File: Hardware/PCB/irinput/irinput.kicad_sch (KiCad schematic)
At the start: 38 parts, among them J1 AudioJack3, J2 Synth_power_2x5, J3 Conn_01x06, J4 Conn_01x06, J5 AudioJack2, J6 AudioJack2, Q1 TOPS-050, SW1 SW_DPDT_x2, SW2 SW_SPDT, U1 TL074

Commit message: Revised schematic to buffer input to variable gain stage
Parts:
- removed C1: 1uF, ao_tht:C_Rect_L7.2mm_W7.2mm_P5.00mm_FKS2_FKP2_MKS2_MKP2, symbol ao_symbols:C
- removed J1: AudioJack3, ao_tht:Jack_6.35mm_PJ_629HAN, symbol ao_symbols:AudioJack3
- removed Q1: TOPS-050, ao_tht:LED_D5.0mm, symbol Device:Q_Photo_NPN
- removed R1: 100R, ao_tht:R_Axial_DIN0207_L6.3mm_D2.5mm_P10.16mm_Horizontal, symbol ao_symbols:R
- removed R12: 2.2k, ao_tht:R_Axial_DIN0207_L6.3mm_D2.5mm_P10.16mm_Horizontal, symbol ao_symbols:R
- removed R2: 10R, ao_tht:R_Axial_DIN0207_L6.3mm_D2.5mm_P10.16mm_Horizontal, symbol ao_symbols:R
- removed R3: 100k, ao_tht:R_Axial_DIN0207_L6.3mm_D2.5mm_P10.16mm_Horizontal, symbol ao_symbols:R
- removed R4: 10k, ao_tht:R_Axial_DIN0207_L6.3mm_D2.5mm_P10.16mm_Horizontal, symbol ao_symbols:R
- removed RV1: A1M, ao_tht:Potentiometer_Alpha_RD901F-40-00D_Single_Vertical_centered, symbol ao_symbols:R_POT
- removed SW2: SW_SPDT, ao_tht:SPDT-toggle-switch-1M-series, symbol ao_symbols:SW_SPDT
- removed unit 4 of U1
- added C?: 1uF, ao_tht:C_Rect_L7.2mm_W7.2mm_P5.00mm_FKS2_FKP2_MKS2_MKP2, symbol ao_symbols:C
- added H1, H2, H3, H4: MountingHole, ao_tht:MountingHole_3.2mm_M3, symbol ao_symbols:MountingHole
- added J?: AudioJack3, ao_tht:Jack_6.35mm_PJ_629HAN, symbol ao_symbols:AudioJack3
- added Q?: TOPS-050, ao_tht:LED_D5.0mm, symbol Device:Q_Photo_NPN
- added R?: 100R, ao_tht:R_Axial_DIN0207_L6.3mm_D2.5mm_P10.16mm_Horizontal, symbol ao_symbols:R
- added R?: 10k, ao_tht:R_Axial_DIN0207_L6.3mm_D2.5mm_P10.16mm_Horizontal, symbol ao_symbols:R
- added R? (x2): 100k, ao_tht:R_Axial_DIN0207_L6.3mm_D2.5mm_P10.16mm_Horizontal, symbol ao_symbols:R
- added R?: 10R, ao_tht:R_Axial_DIN0207_L6.3mm_D2.5mm_P10.16mm_Horizontal, symbol ao_symbols:R
- added RV?: A1M, ao_tht:Potentiometer_Alpha_RD901F-40-00D_Single_Vertical_centered, symbol ao_symbols:R_POT
- added SW2: SW_DPDT_x2, ao_tht:DPDT-toggle-switch-1M-seriesx, symbol Switch:SW_DPDT_x2
- added U?: TL074, ao_tht:DIP-14_W7.62mm_Socket_LongPads, symbol ao_symbols:TL074
- R5, R6: value 10k -> 1k
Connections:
- net EMIT is gone; now on net DC: SW1.5 (B)
- net +12V: now also R?.1
- net AC: now also R?.1, SW2.3 (C)
- net COLL: now also R?.2
- net CV_LED_1: now also U1.14
- net CV_LED_1_P: now also D5.1 (KA); no longer D5.2 (AK)
- net CV_LED_2: now also R6.1, R8.1, U1.9 (-)
- net CV_LED_2_P: now also D5.2 (AK); no longer D5.1 (KA)
- net DC: now also C?.1, R?.1, SW2.1 (A)
- net EXT_C: now also J?.T
- net EXT_E: now also J?.R
- net GND: now also U1.12 (+), J?.S, R?.2, RV?.1; no longer U1.3 (+)
- net SENSITIVITY: now also R?.2, RV?.2, RV?.3
- net at RV2.2, RV2.3, U1.6 (-): now also R?.1, R?.1
- net at SW1.1 (A): now also Q?.1 (C)
- net at R5.1, R6.2: now also U1.13 (-); no longer U1.2 (-)
- net at SW1.4 (A): now also Q?.2 (E)
- new net: C?.2, SW2.2 (B), U?.3 (+)
- new net: R?.2, SW2.6 (C)
- new net: R?.2, SW2.4 (A)
- new net BUF: SW2.5 (B), U?.1, U?.2 (-)
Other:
- note added: "Inverting stages with variable gain added"
- note added: "Jacks/LEDs board"
- note removed: "Originally was fixed unity gain"
- moved on the sheet: D3, D4, D5, J3, J4, J5, J6, R10, R11, R5, R6, R7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

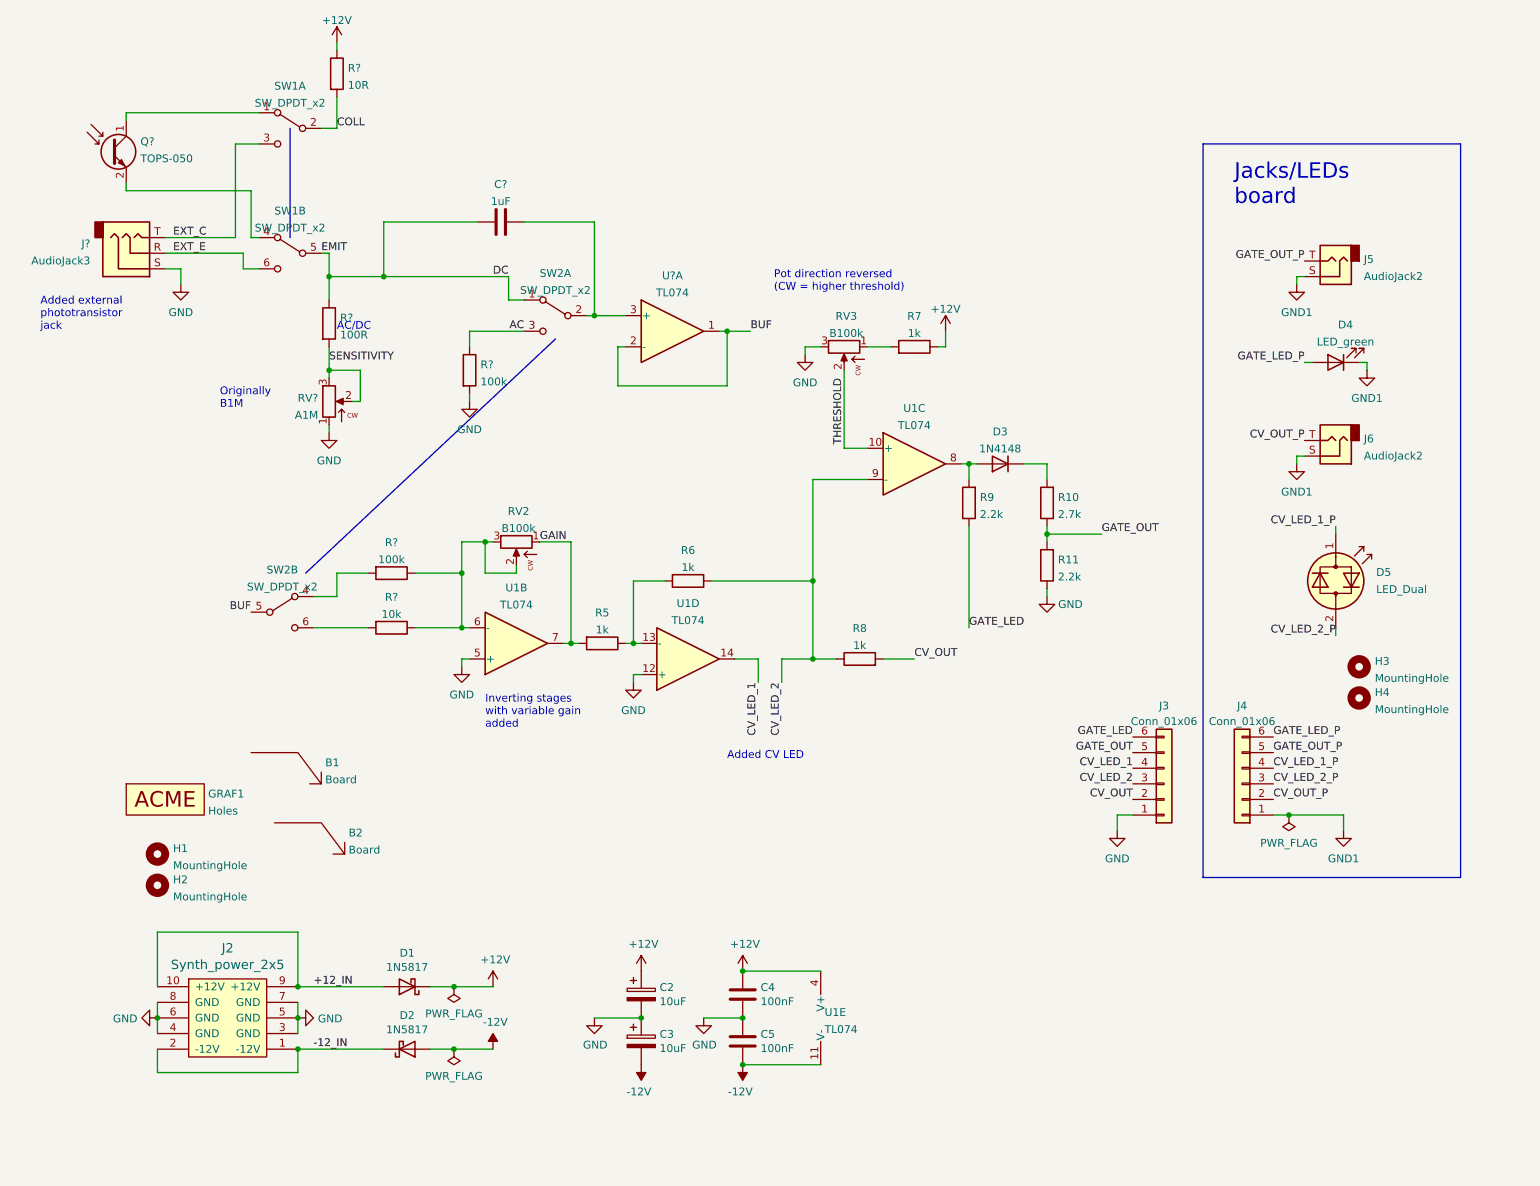
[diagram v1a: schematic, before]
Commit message: Revert to using no inverting stages, put gain control on non inverting stage. Add saturation LED.
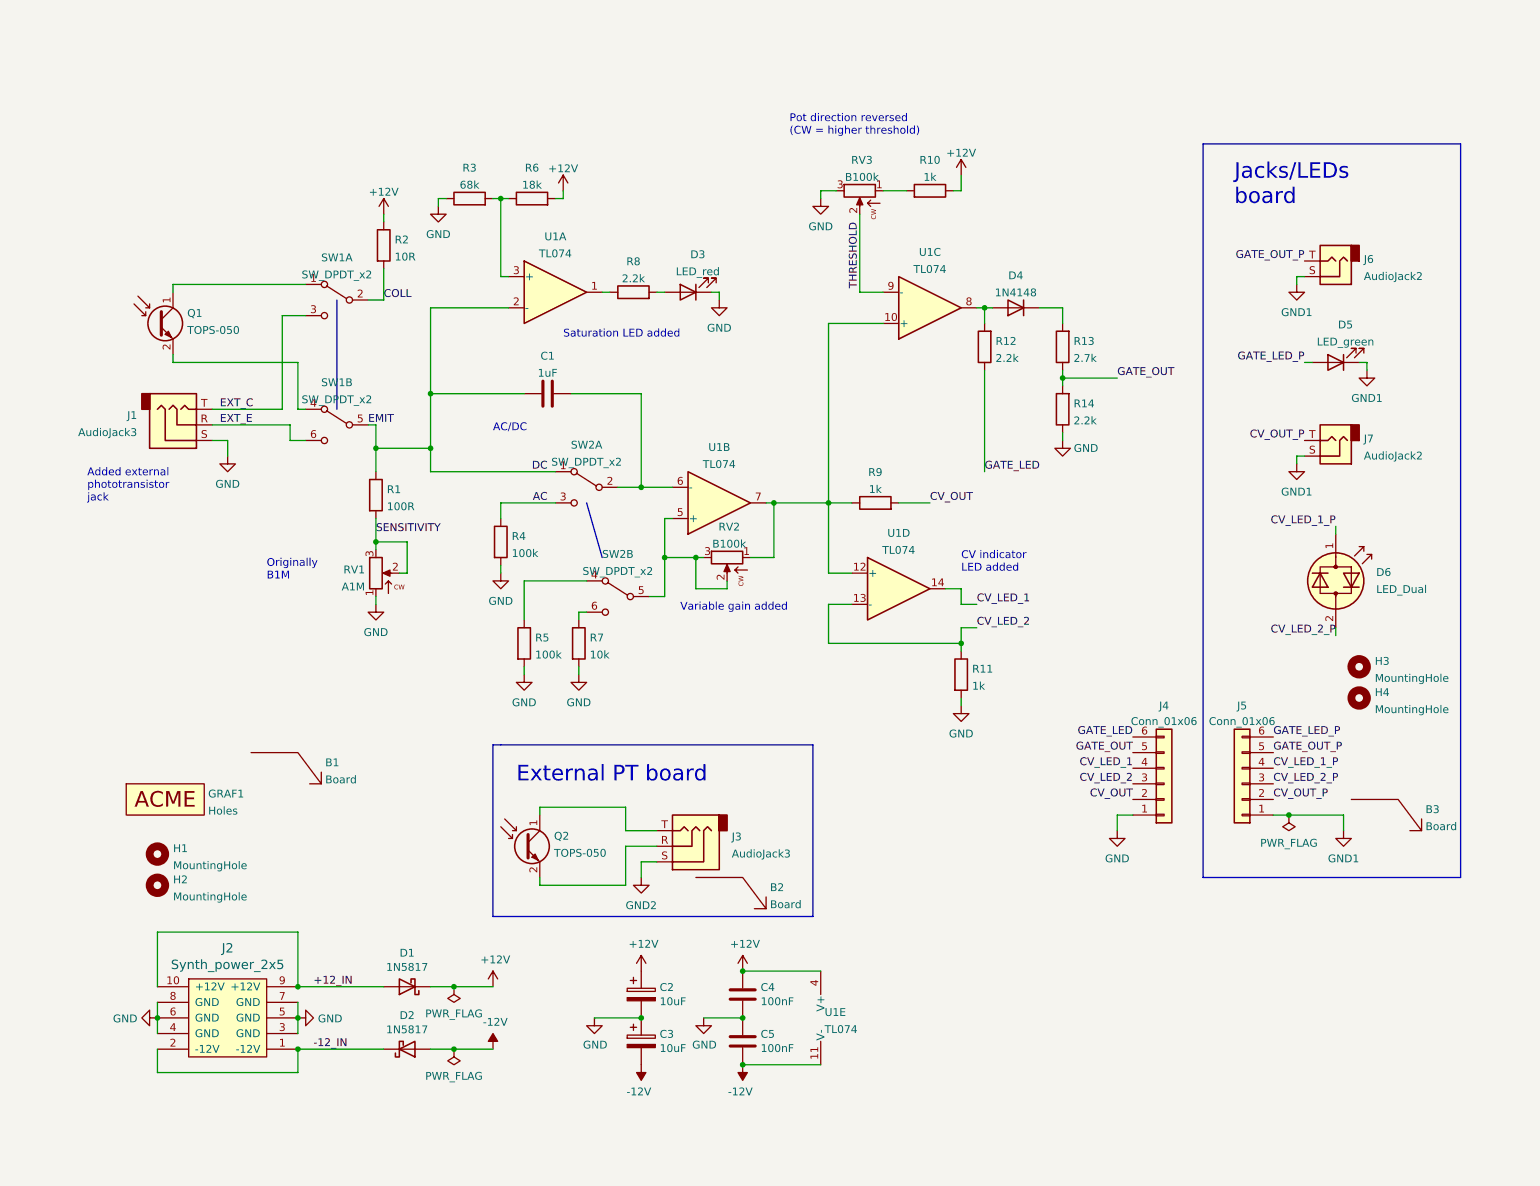
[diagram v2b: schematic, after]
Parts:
- removed R?: 10k, ao_tht:R_Axial_DIN0207_L6.3mm_D2.5mm_P10.16mm_Horizontal, symbol ao_symbols:R
- removed R?: 100k, ao_tht:R_Axial_DIN0207_L6.3mm_D2.5mm_P10.16mm_Horizontal, symbol ao_symbols:R
- added B2: Board, ao_tht:Board_Marker, symbol ao_symbols:Board
- added D3: LED_red, ao_tht:LED_D5.0mm, symbol ao_symbols:LED_red
- added J3: AudioJack3, ao_tht:Jack_3.5mm_PJ-301CM, symbol ao_symbols:AudioJack3
- added Q2: TOPS-050, ao_tht:LED_D5.0mm, symbol Device:Q_Photo_NPN
- added R11: 1k, ao_tht:R_Axial_DIN0207_L6.3mm_D2.5mm_P10.16mm_Horizontal, symbol ao_symbols:R
- added R3: 68k, ao_tht:R_Axial_DIN0207_L6.3mm_D2.5mm_P10.16mm_Horizontal, symbol ao_symbols:R
- added R7: 10k, ao_tht:R_Axial_DIN0207_L6.3mm_D2.5mm_P10.16mm_Horizontal, symbol ao_symbols:R
- added R8: 2.2k, ao_tht:R_Axial_DIN0207_L6.3mm_D2.5mm_P10.16mm_Horizontal, symbol ao_symbols:R
- J1: renamed from J?; footprint ao_tht:Jack_6.35mm_PJ_629HAN -> ao_tht:Jack_3.5mm_PJ-301CM
- R5: value 1k -> 100k
- R6: value 1k -> 18k
- gave numbers to parts that had none: 7
- renumbered B2 to B3, D3 to D4, D4 to D5, D5 to D6, J3 to J4, J4 to J5, J5 to J6, J6 to J7, R7 to R10, R9 to R12, R10 to R13, R11 to R14, R8 to R9
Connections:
- net +12V: now also R6.2
- net CV_LED_2: now also U1.13 (-), R11.1; no longer R6.1, R9.1, U1.9 (-)
- net DC: now also U1.2 (-)
- net GND: now also R5.2, D3.1 (K), R11.2, R3.1, R7.2; no longer U1.12 (+), U1.5 (+)
- net THRESHOLD: now also U1.9 (-); no longer U1.10 (+)
- net at C1.2, SW2.2 (B): now also U1.6 (-); no longer U1.3 (+)
- net at RV2.2, RV2.3: now also SW2.5 (B), U1.5 (+); no longer U1.6 (-)
- net at SW2.6 (C): now also R7.1
- net at SW2.4 (A): now also R5.1
- removed net BUF: SW2.5 (B), U1.1, U1.2 (-)
- net GAIN: no longer names the net of RV2.1, U1.7
- net GAIN: now also R9.1, U1.10 (+), U1.12 (+); no longer R5.2
- new net: R8.1, U1.1
- new net: R3.2, R6.1, U1.3 (+)
- new net: D3.2 (A), R8.2
- new net: J3.R, Q2.2 (E)
- new net: J3.T, Q2.1 (C)
- new net GND2: J3.S
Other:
- note added: "CV indicator LED added"
- note added: "External PT board"
- note added: "Saturation LED added"
- note added: "Variable gain added"
- note removed: "Added CV LED"
- note removed: "Inverting stages with variable gain added"
- moved on the sheet: B3, C1, D4, J1, Q1, R1, R10, R12, R13, R14, R2, R4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

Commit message: Corrections
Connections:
- net DC: now also U1.3 (+); no longer U1.2 (-)
- net at R3.2, R6.1: now also U1.2 (-); no longer U1.3 (+)
- net at C1.2, SW2.2 (B): now also U1.5 (+); no longer U1.6 (-)
- net at RV2.2, RV2.3, SW2.5 (B): now also U1.6 (-); no longer U1.5 (+)
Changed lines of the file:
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@@
     )
   )
-  (symbol (lib_id "ao_symbols:TL074") (at 104.14 59.69 0) (unit 1)
+  (symbol (lib_id "ao_symbols:TL074") (at 104.14 59.69 0) (mirror x) (unit 1)
     (in_bom yes) (on_board yes) (fields_autoplaced)
     (property "Reference" "U1" (id 0) (at 104.14 50.6435 0))
     (property "Value" "TL074" (id 1) (at 104.14 53.4186 0))
-    (property "Footprint" "ao_tht:DIP-14_W7.62mm_Socket_LongPads" (id 2) (at 102.87 57.15 0)
-      (effects (font (size 1.27 1.27)) hide)
-    )
-    (property "Datasheet" "" (id 3) (at 105.41 54.61 0)
+    (property "Footprint" "ao_tht:DIP-14_W7.62mm_Socket_LongPads" (id 2) (at 102.87 62.23 0)
+      (effects (font (size 1.27 1.27)) hide)
+    )
+    (property "Datasheet" "" (id 3) (at 105.41 64.77 0)
       (effects (font (size 1.27 1.27)) hide)
     )
@@
     (pin "1")
   )
-  (symbol (lib_id "ao_symbols:TL074") (at 130.81 93.98 0) (mirror x) (unit 2)
+  (symbol (lib_id "ao_symbols:TL074") (at 130.81 93.98 0) (unit 2)
     (in_bom yes) (on_board yes) (fields_autoplaced)
     (property "Reference" "U1" (id 0) (at 130.81 84.9335 0))
     (property "Value" "TL074" (id 1) (at 130.81 87.7086 0))
-    (property "Footprint" "ao_tht:DIP-14_W7.62mm_Socket_LongPads" (id 2) (at 129.54 96.52 0)
-      (effects (font (size 1.27 1.27)) hide)
-    )
-    (property "Datasheet" "" (id 3) (at 132.08 99.06 0)
-      (effects (font (size 1.27 1.27)) hide)
-    )
+    (property "Footprint" "ao_tht:DIP-14_W7.62mm_Socket_LongPads" (id 2) (at 129.54 91.44 0)
+      (effects (font (size 1.27 1.27)) hide)
+    )
+    (property "Datasheet" "" (id 3) (at 132.08 88.9 0)
+      (effects (font (size 1.27 1.27)) hide)
+    )

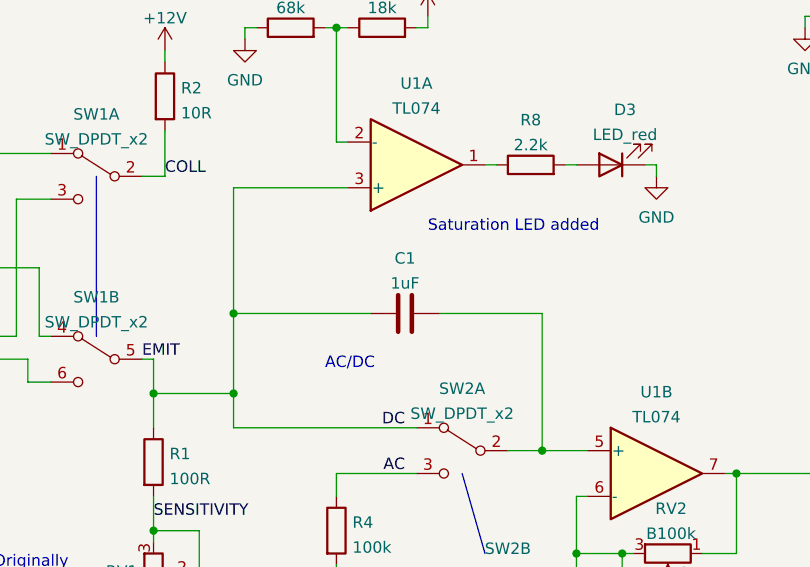
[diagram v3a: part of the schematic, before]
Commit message: Corrected cap, initial BOM
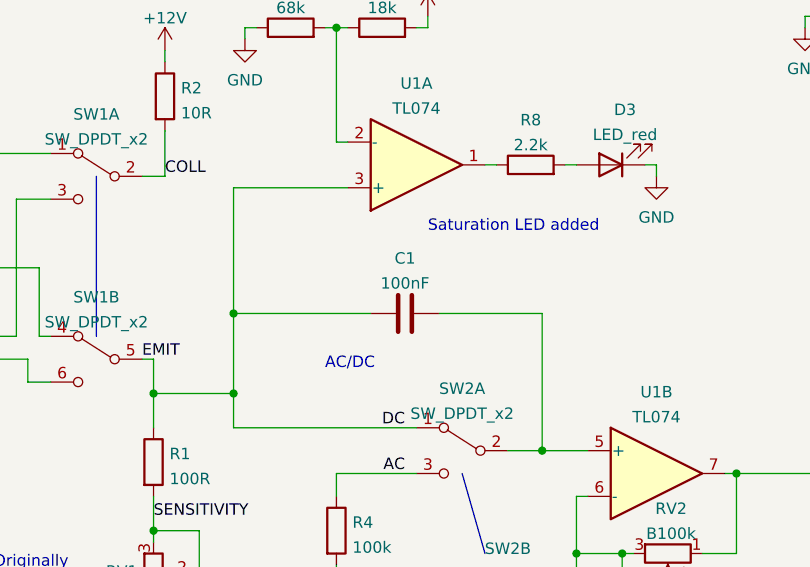
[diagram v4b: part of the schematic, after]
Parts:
- C1: value 1uF -> 100nF
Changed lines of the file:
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@@
     (in_bom yes) (on_board yes) (fields_autoplaced)
     (property "Reference" "C1" (id 0) (at 102.87 70.0745 90))
-    (property "Value" "1uF" (id 1) (at 102.87 72.8496 90))
+    (property "Value" "100nF" (id 1) (at 102.87 72.8496 90))
     (property "Footprint" "ao_tht:C_Rect_L7.2mm_W7.2mm_P5.00mm_FKS2_FKP2_MKS2_MKP2" (id 2) (at 106.68 75.2348 0)
       (effects (font (size 1.27 1.27)) hide)
@@
     )
     (path "/2f5f9a85-d35f-44b8-95b6-8a5486a2748e"
-      (reference "C1") (unit 1) (value "1uF") (footprint "ao_tht:C_Rect_L7.2mm_W7.2mm_P5.00mm_FKS2_FKP2_MKS2_MKP2")
+      (reference "C1") (unit 1) (value "100nF") (footprint "ao_tht:C_Rect_L7.2mm_W7.2mm_P5.00mm_FKS2_FKP2_MKS2_MKP2")
     )
     (path "/00000000-0000-0000-0000-00005f73fa30"

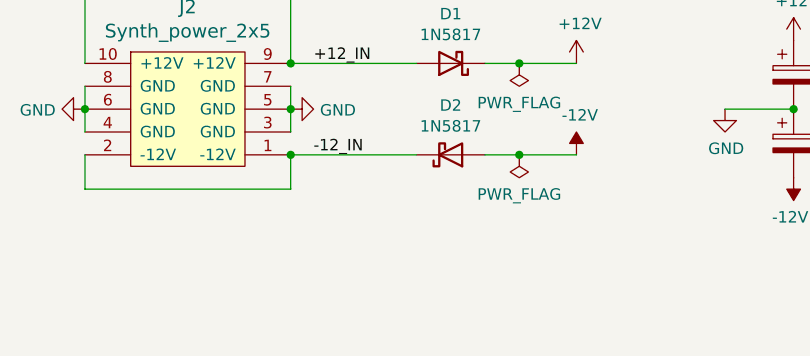
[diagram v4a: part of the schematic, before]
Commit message: Silkscreen cleanup, revised panel
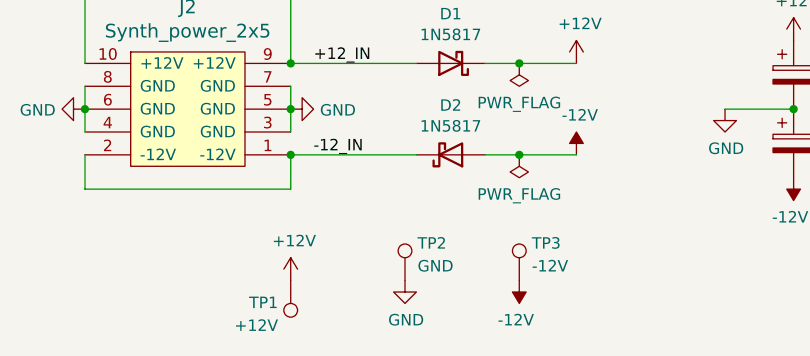
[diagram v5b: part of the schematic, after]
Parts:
- added TP1: +12V, ao_tht:TestPoint_THTPad_D1.5mm_Drill0.7mm, symbol ao_symbols:TestPoint
- added TP2: GND, ao_tht:TestPoint_THTPad_D1.5mm_Drill0.7mm, symbol ao_symbols:TestPoint
- added TP3: -12V, ao_tht:TestPoint_THTPad_D1.5mm_Drill0.7mm, symbol ao_symbols:TestPoint
- C1: footprint ao_tht:C_Rect_L7.2mm_W7.2mm_P5.00mm_FKS2_FKP2_MKS2_MKP2 -> ao_tht:C_Rect_L7.2mm_W2.5mm_P5.00mm_FKS2_FKP2_MKS2_MKP2
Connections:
- net +12V: now also TP1.1
- net -12V: now also TP3.1
- net GND: now also TP2.1

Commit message: Catch up to 1st fab run version
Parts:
- removed B2: Board, ao_tht:Board_Marker, symbol ao_symbols:Board
- B1, B3, GRAF1: now left out of the parts list
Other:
- note added: "External PT"
- note removed: "External PT board"
- note removed: "Pot direction reversed (CW = higher threshold)"
